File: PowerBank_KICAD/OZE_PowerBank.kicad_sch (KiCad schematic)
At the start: 84 parts, among them IC1 TPS2514ADBVT, IC3 TPS25810RVCR, J1 Conn_01x02_Pin, J10 Conn_01x04_Pin, J11 Conn_01x02_Pin, J12 Battery with BMS Input, J2 DCJ200-10-A-XX-K_REVA, J3 Conn_01x04_Pin, J4 Conn_01x04_Pin, J5 Conn_01x04_Pin, J6 Conn_01x10_Pin, J7 USB_A, J8 USB_C_Receptacle_PowerOnly_6P, J9 Conn_01x04_Pin, Q1 PMOS, Q2 IRLZ44N, Q3 IRLZ44N, SW1 SW_Push, SW2 SW_SPDT, U1 TLV70233_SOT23-5, U2 STM32F103C8Tx, U3 LM5106SD, U5 INA180A2, Y1 16MHz

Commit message: added footprints, i have libraries localy, give comments about calculations of elements
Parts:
- added C32: 100n, Capacitor_SMD:C_0805_2012Metric_Pad1.18x1.45mm_HandSolder, symbol Device:C_Small
- added J13: Conn_01x10_Pin, symbol Connector:Conn_01x10_Pin
- C1, C11, C12, C14, C15, C16, C17, C18, C19, C2, C20, C21, C22, C23, C25, C26, C27, C28, C3, C30, C31, C4, C5, C6, C7, C8, C9: footprint (none) -> Capacitor_SMD:C_0805_2012Metric_Pad1.18x1.45mm_HandSolder
- C10: value 22u -> 22uF; footprint (none) -> Capacitor_SMD:C_0805_2012Metric_Pad1.18x1.45mm_HandSolder
- D1: value LED -> BLUE; footprint (none) -> LED_SMD:LED_1206_3216Metric_Pad1.42x1.75mm_HandSolder
- D2: footprint (none) -> LED_SMD:LED_1206_3216Metric_Pad1.42x1.75mm_HandSolder
- R1: value 10k -> 47; footprint (none) -> Resistor_SMD:R_0805_2012Metric_Pad1.20x1.40mm_HandSolder
- R10, R11, R12, R13, R15, R16, R2, R3, R4, R5, R7: footprint (none) -> Resistor_SMD:R_0805_2012Metric_Pad1.20x1.40mm_HandSolder
- R14: footprint (none) -> Resistor_SMD:R_1206_3216Metric_Pad1.30x1.75mm_HandSolder
- R6: value 1k5 -> 100R; footprint (none) -> Resistor_SMD:R_0805_2012Metric_Pad1.20x1.40mm_HandSolder
- R8: value 91k -> 9k1; footprint (none) -> Resistor_SMD:R_0805_2012Metric_Pad1.20x1.40mm_HandSolder
- R9: value 10k -> 1k; footprint (none) -> Resistor_SMD:R_0805_2012Metric_Pad1.20x1.40mm_HandSolder
- SW2: footprint (none) -> LIB_SLW-1276864-4A-D:SLW12768644AD
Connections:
- net +3.3V: now also C32.1
- net CHG: now also J13.6 (Pin_6)
- net CHG_HI: now also J13.7 (Pin_7)
- net ENABLE: now also J13.1 (Pin_1)
- net GND: now also C32.2
- net I_OUT: now also J13.5 (Pin_5)
- net PWM: now also J13.2 (Pin_2)
- net V_BAT: now also J13.4 (Pin_4)
- net V_beforeBUCK: now also J13.3 (Pin_3)
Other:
- note added: "10/(9,1+1) = 0,099 VinMAX = 21V; VoutMAX = 21.0 * 0,099099 = 2.0792 V Rth = 901 Ohm; Imax = 2.08 mA; P = 43,7mW; rezystory 1/8W"
- note added: "8.4V"
- note added: "LED - 20mA Vfarward = 3.2 V R=(Vzas-Vf)/If = 20Ohm -> 47 Ohm"
- note added: "Spare STM Pins, Debug Pins"
- note added: "Uwej = 16 V Iwej = 0.5A"
- note added: "Vadc = Vin * R2/(R2+R1) = 8,4*10/(27+10) = 2,189 V"
- note added: "Vforw = 2V R=(3,3-2)/0,015 = 89Ohm -> 100Ohm"
- note added: "Vout = I*Rshunt*Gwzm 3.3 = 1 * Rsh * 50 Rsh = 3.3/50 = 66mOhm dla Rsh = 50 mOhm - max 2,5 V P = I^2*R = 1*0,050 = 0.05W"
- note added: "u = 85% Pin = 8W Pout = Pin * u = 6.8 W Iout = Pout/Vout = 0,81 A"
- note removed: "Spare STM Pins"
- moved on the sheet: R8, R9

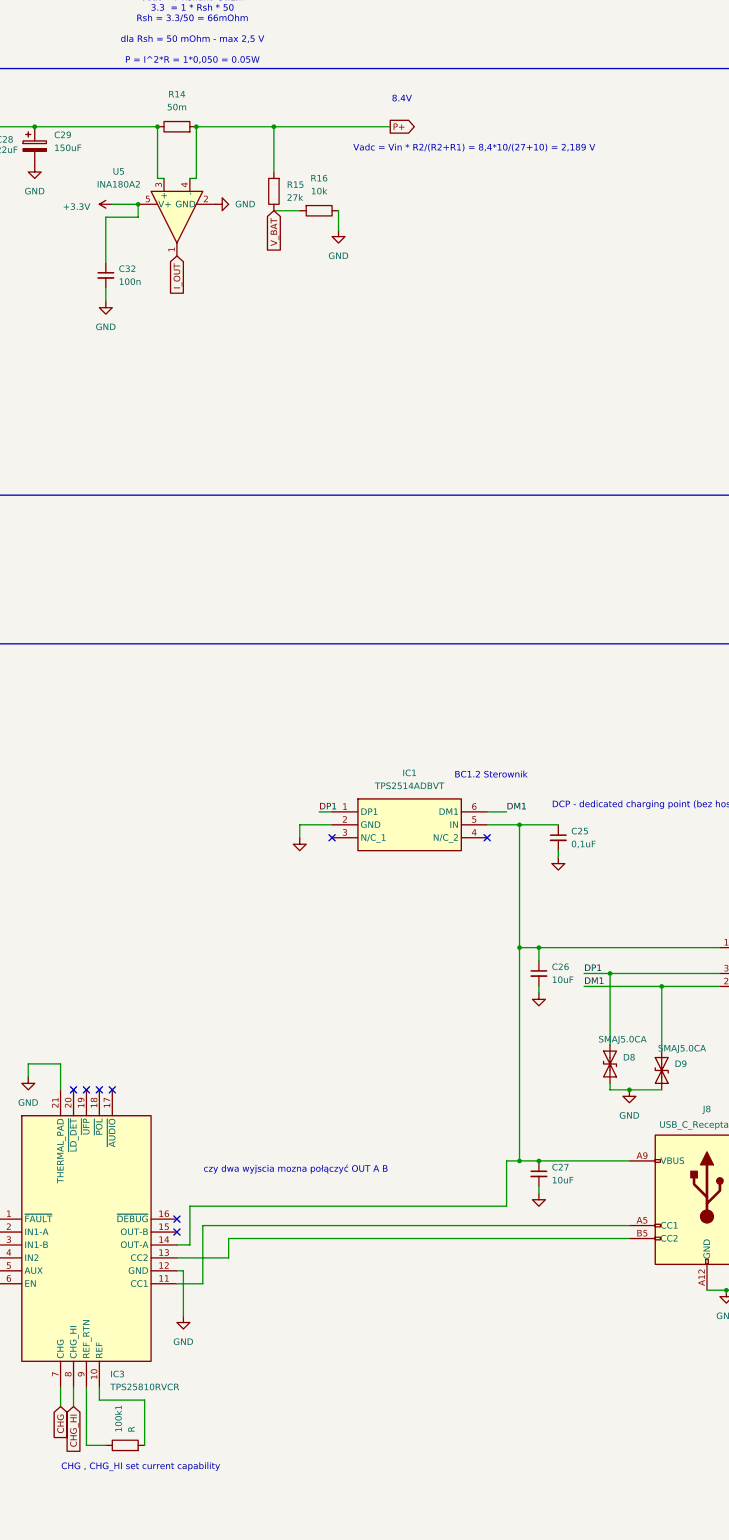
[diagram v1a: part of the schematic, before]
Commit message: Zmiany na schemacie
Zmiana wzmacniacza z INA180A2 na INA180A1 bo za duże napięcie wychodziło na wyjściu i wywaliłem symulacje bo bez niej nie moge dac commita
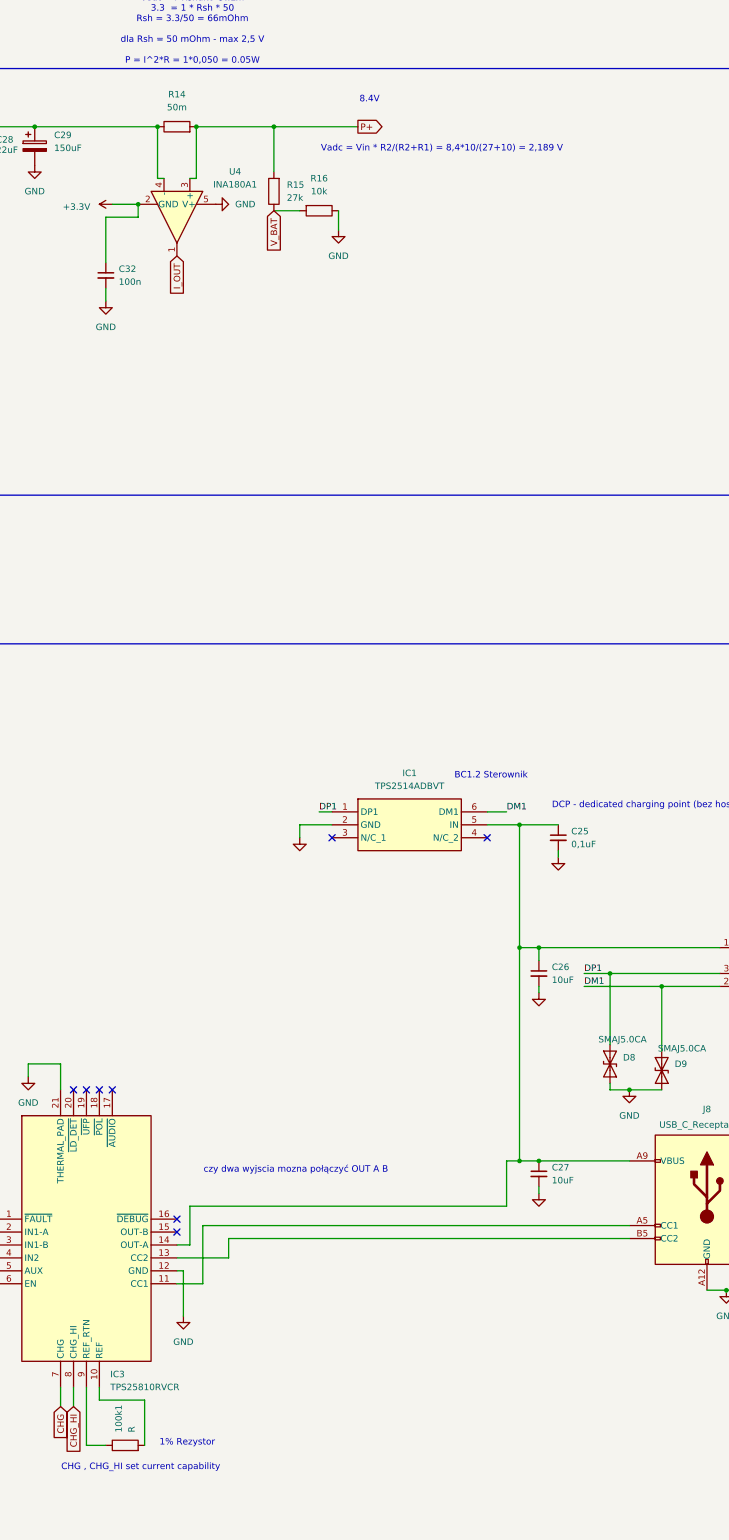
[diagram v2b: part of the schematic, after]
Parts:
- removed U5: INA180A2, Package_TO_SOT_SMD:SOT-23-5, symbol Amplifier_Current:INA180A2
- added U4: INA180A1, Package_TO_SOT_SMD:SOT-23-5, symbol Amplifier_Current:INA180A1
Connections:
- net +3.3V: now also U4.2 (GND)
- net GND: now also U4.5 (V+)
- net I_OUT: now also U4.1
- net P+: now also U4.3 (+)
- net at C28.1, C29.1, L1.2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: now also U4.4 (-)
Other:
- note added: "1% Rezystor"
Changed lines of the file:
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@@
 		)
 	)
+	(text "1% Rezystor"
+		(exclude_from_sim no)
+		(at 452.882 304.292 0)
+		(effects
+			(font
+				(size 1.27 1.27)
+			)
+		)
+	)
 	(text "Uwej = 16 V Iwej = 0.5A\n"
 		(exclude_from_sim no)
@@
 	(text "Vadc = Vin * R2/(R2+R1) = 8,4*10/(27+10) = 2,189 V "
 		(exclude_from_sim no)
-		(at 509.27 50.038 0)
+		(at 502.92 50.038 0)
 		(effects
 			(font
@@
 	(text "8.4V"
 		(exclude_from_sim no)
-		(at 495.046 40.386 0)
+		(at 488.696 40.386 0)
 		(effects
 			(font
@@
 	)
 	(junction
-		(at 443.23 60.96)
-		(diameter 0)
-		(color 0 0 0 0)
-	)
-	(junction
 		(at 73.66 64.77)
 		(diameter 0)
@@
 	)
 	(junction
+		(at 443.23 60.96)
+		(diameter 0)
+		(color 0 0 0 0)
+	)
+	(junction
 		(at 605.79 53.34)
 		(diameter 0)
@@
 	(wire
 		(pts
-			(xy 469.9 45.72) (xy 492.76 45.72)
-		)
-		(stroke
-			(width 0)
-			(type default)
-		)
-	)
-	(wire
-		(pts
 			(xy 139.7 260.35) (xy 139.7 271.78)
 		)
@@
 	(wire
 		(pts
+			(xy 469.9 45.72) (xy 486.41 45.72)
+		)
+		(stroke
+			(width 0)
+			(type default)
+		)
+	)
+	(wire
+		(pts
 			(xy 69.85 69.85) (xy 76.2 69.85)
 		)
@@
 	(global_label "P+"
 		(shape output)
-		(at 492.76 45.72 0)
+		(at 486.41 45.72 0)
 		(fields_autoplaced yes)
 		(effects
@@
 		)
 		(property "Intersheetrefs" "${INTERSHEET_REFS}"
-			(at 498.5876 45.72 0)
+			(at 492.2376 45.72 0)
 			(effects
 				(font
@@
 	)
 	(symbol
-		(lib_id "Amplifier_Current:INA180A2")
-		(at 450.85 63.5 90)
-		(mirror x)
-		(unit 1)
-		(exclude_from_sim no)
-		(in_bom yes)
-		(on_board yes)
-		(dnp no)
-		(fields_autoplaced yes)
-		(property "Reference" "U5"
-			(at 439.42 54.5398 90)
-			(effects
-				(font
-					(size 1.27 1.27)
-				)
-			)
-		)
-		(property "Value" "INA180A2"
-			(at 439.42 57.0798 90)
-			(effects
-				(font
-					(size 1.27 1.27)
-				)
-			)
-		)
-		(property "Footprint" "Package_TO_SOT_SMD:SOT-23-5"
-			(at 449.58 64.77 0)
-			(effects
-				(font
-					(size 1.27 1.27)
-				)
-				(hide yes)
-			)
-		)
-		(property "Datasheet" "http://www.ti.com/lit/ds/symlink/ina180.pdf"
-			(at 447.04 67.31 0)
-			(effects
-				(font
-					(size 1.27 1.27)
-				)
-				(hide yes)
-			)
-		)
-		(property "Description" "Current Sense Amplifier, 1 Circuit, Rail-to-Rail, 26V, Gain 50 V/V, SOT-23-5"
-			(at 450.85 63.5 0)
-			(effects
-				(font
-					(size 1.27 1.27)
-				)
-				(hide yes)
-			)
-		)
-		(pin "3"
-		)
-		(pin "2"
-		)
-		(pin "4"
-		)
-		(pin "5"
-		)
-		(pin "1"
-		)
-		(instances
-			(project "OZE_PowerBank"
-				(path "/05ef670e-1266-4770-84e3-f6b3d153fd91"
-					(reference "U5")
-					(unit 1)
-				)
-			)
-		)
-	)
-	(symbol
 		(lib_id "TPS2514ADBVT:TPS2514ADBVT")
 		(at 481.33 180.34 0)
@@
 					(unit 1)
 				)
+			)
+		)
+	)
+	(symbol
+		(lib_id "Amplifier_Current:INA180A1")
+		(at 450.85 63.5 270)
+		(unit 1)
+		(exclude_from_sim no)
+		(in_bom yes)
+		(on_board yes)
+		(dnp no)
+		(fields_autoplaced yes)
+		(property "Reference" "U4"
+			(at 462.28 54.5398 90)
+			(effects
+				(font
+					(size 1.27 1.27)
+				)
+			)
+		)
+		(property "Value" "INA180A1"
+			(at 462.28 57.0798 90)
+			(effects
+				(font
+					(size 1.27 1.27)
+				)
+			)
+		)
+		(property "Footprint" "Package_TO_SOT_SMD:SOT-23-5"
+			(at 452.12 64.77 0)
+			(effects
+				(font
+					(size 1.27 1.27)
+				)
+				(hide yes)
+			)
+		)
+		(property "Datasheet" "http://www.ti.com/lit/ds/symlink/ina180.pdf"
+			(at 454.66 67.31 0)
+			(effects
+				(font
+					(size 1.27 1.27)
+				)
+				(hide yes)
+			)
+		)
+		(property "Description" "Current Sense Amplifier, 1 Circuit, Rail-to-Rail, 26V, Gain 20 V/V, SOT-23-5"
+			(at 450.85 63.5 0)
+			(effects
+				(font
+					(size 1.27 1.27)
+				)
+				(hide yes)
+			)
+		)
+		(pin "1"
+		)
+		(pin "3"
+		)
+		(pin "4"
+		)
+		(pin "5"
+		)
+		(pin "2"
+		)
+		(instances
+			(project ""
+				(path "/05ef670e-1266-4770-84e3-f6b3d153fd91"
+					(reference "U4")
+					(unit 1)
+				)
